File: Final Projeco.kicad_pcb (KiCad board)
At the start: 2 copper layers, 1 part, among them U1 ESP32-S3

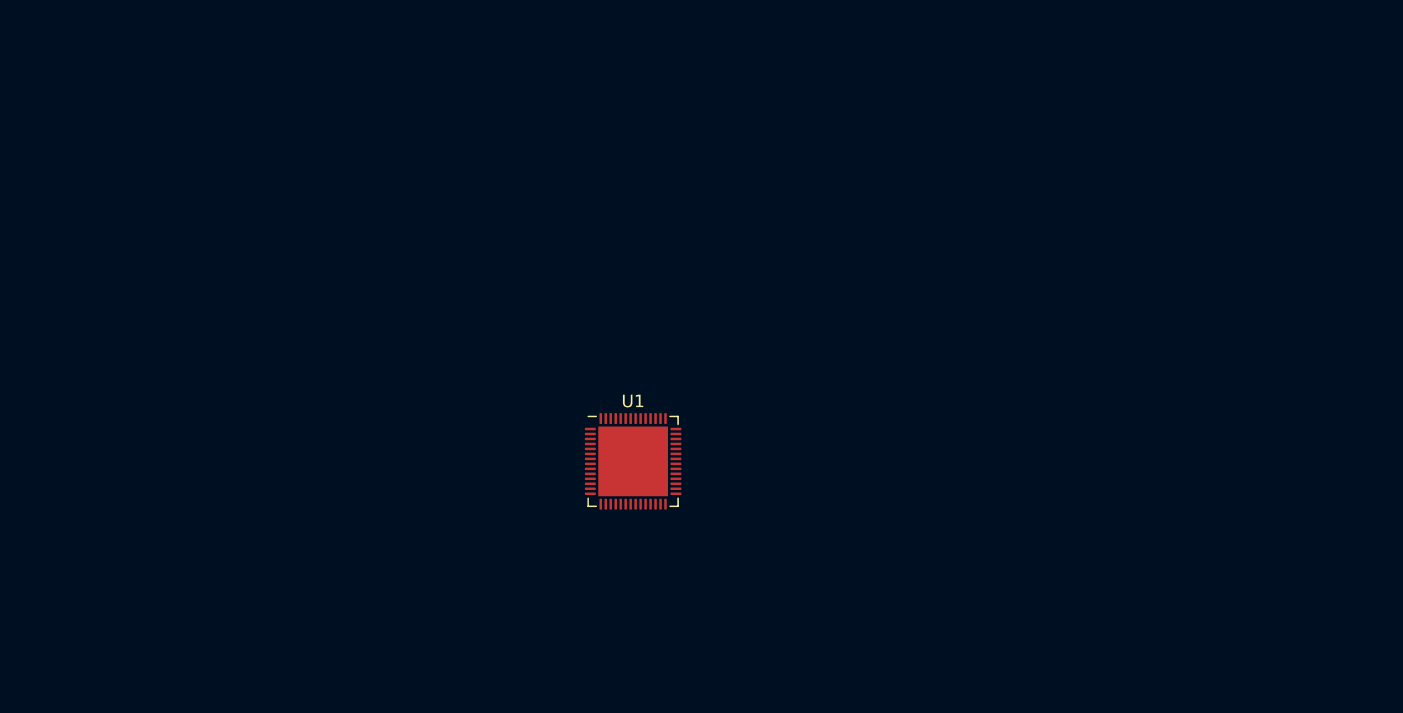
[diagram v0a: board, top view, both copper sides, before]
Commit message: -USE IPEX 2.4 GHz Antenna
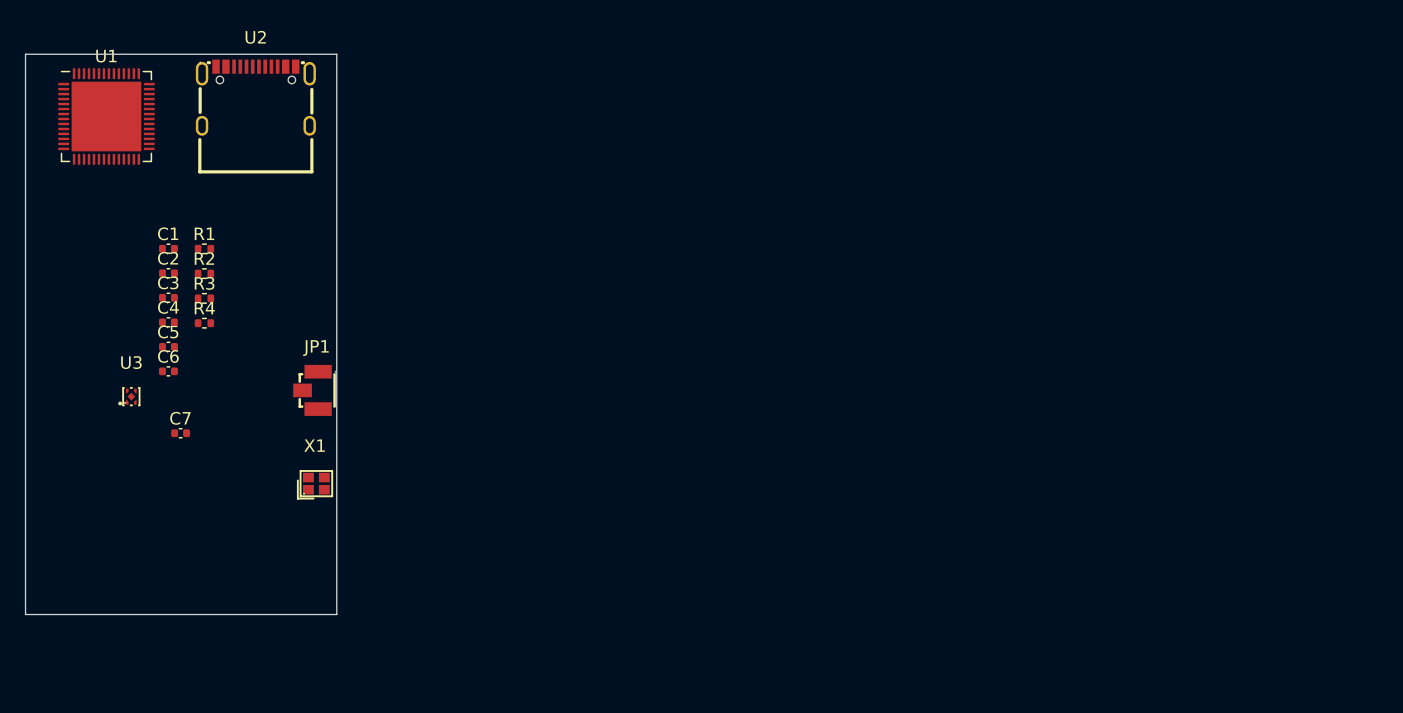
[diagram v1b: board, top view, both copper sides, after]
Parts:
- added C1: C, Capacitor_SMD:C_0402_1005Metric, F.Cu at (38.0, 31.1)
- added C2: C, Capacitor_SMD:C_0402_1005Metric, F.Cu at (38.0, 33.1)
- added C3: 1uF, Capacitor_SMD:C_0402_1005Metric, F.Cu at (38.0, 35.1)
- added C4: C, Capacitor_SMD:C_0402_1005Metric, F.Cu at (38.0, 37.0)
- added C5: C, Capacitor_SMD:C_0402_1005Metric, F.Cu at (38.0, 39.0)
- added C6: C, Capacitor_SMD:C_0402_1005Metric, F.Cu at (38.0, 41.0)
- added C7: 1uF, Capacitor_SMD:C_0402_1005Metric, F.Cu at (39.0, 45.9)
- added JP1: U_FL-R-SMT-1(10), jlc:ANT-SMD_UFL-R-SMT-1-10, F.Cu at (49.4, 42.5)
- added R1: 10K, Resistor_SMD:R_0402_1005Metric, F.Cu at (40.9, 31.1)
- added R2: 5.1K, Resistor_SMD:R_0402_1005Metric, F.Cu at (40.9, 33.1)
- added R3: 5.1K, Resistor_SMD:R_0402_1005Metric, F.Cu at (40.9, 35.1)
- added R4: 10K, Resistor_SMD:R_0402_1005Metric, F.Cu at (40.9, 37.1)
- added U2: GT-USB-7004N, jlc:USB-C-SMD_GT-USB-7004, F.Cu at (45.0, 18.9)
- added U3: NCP167BMX330TBG, jlc:XDFN-4_L1.0-W1.0-P0.65-BL-EP, F.Cu at (35.0, 43.0)
- added X1: TZ1269D, jlc:CRYSTAL-SMD_4P-L2.0-W1.6-BL-A, F.Cu at (49.9, 50.0)
- moved U1 50.6 mm to (33.0, 20.5)
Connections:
- U1 pad 1: unconnected-(U1-LNA_IN/RF-Pad1) -> Net-(JP1-SIN)
- U1 pad 57: unconnected-(U1-GND-Pad57) -> Net-(U1-GND)
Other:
- board outline added: 25 x 45 mm

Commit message: -Added some Headers
-Added Headers
-TODO (chore) (top priority):
 -    relabel EVERYTHING with net class (line) NOT directive (circle)
 -    get layout fixed
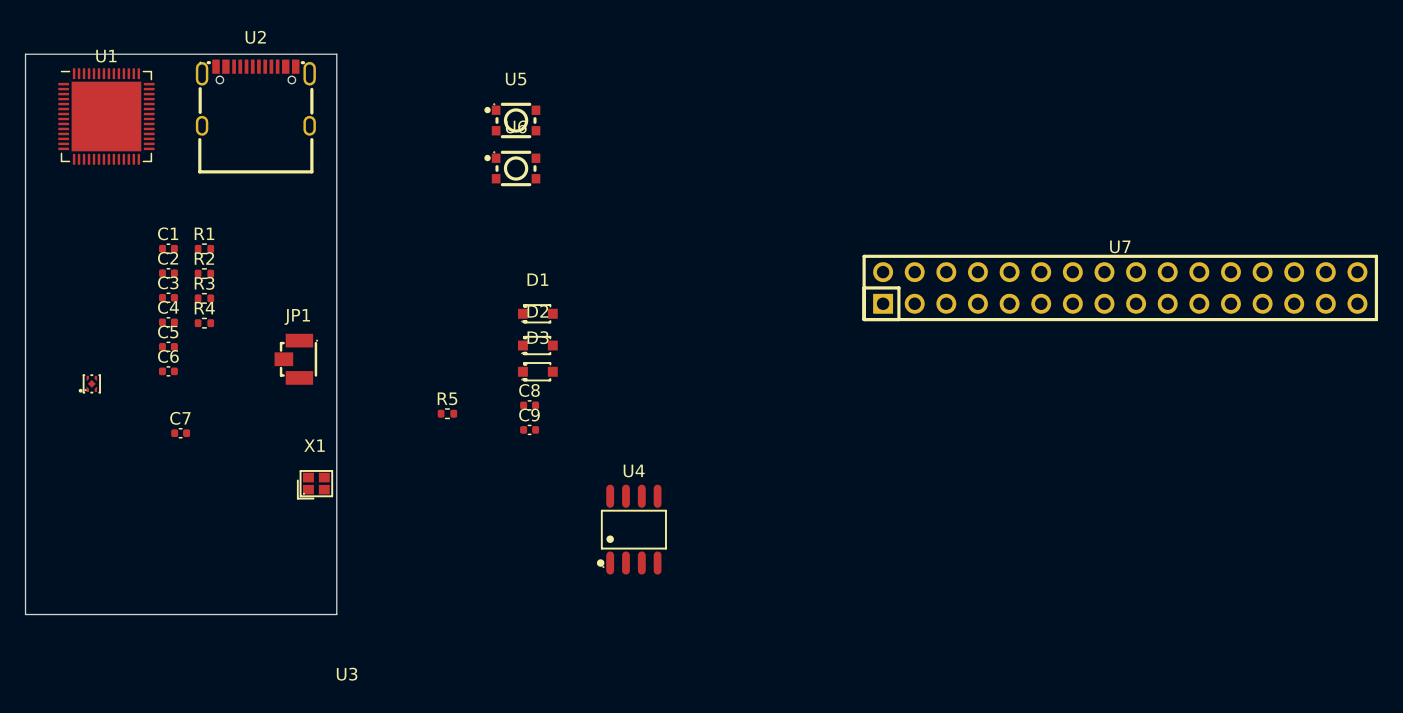
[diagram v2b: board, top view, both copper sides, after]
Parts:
- added C8: 1uF, Capacitor_SMD:C_0402_1005Metric, F.Cu at (67.0, 43.7)
- added C9: 0.1uF, Capacitor_SMD:C_0402_1005Metric, F.Cu at (67.0, 45.7)
- added D1: SD103AWS_C5345966, jlc:SOD-323_L1.7-W1.3-LS2.5-RD, F.Cu at (67.7, 36.3)
- added D2: SD103AWS_C5345966, jlc:SOD-323_L1.7-W1.3-LS2.5-RD, F.Cu at (67.7, 38.9)
- added D3: SD103AWS_C5345966, jlc:SOD-323_L1.7-W1.3-LS2.5-RD, F.Cu at (67.7, 41.0)
- added R5: 100K, Resistor_SMD:R_0402_1005Metric, F.Cu at (60.4, 44.4)
- added U4: LY68L6400SLIT, jlc:SOP-8_L4.9-W3.9-P1.27-LS6.0-BL, F.Cu at (75.4, 53.7)
- added U5: PTS830GG140SMTRLFS, jlc:KEY-SMD_4P-L3.1-W2.6_PTS830GG140SMTRLFS, F.Cu at (65.9, 20.8)
- added U6: PTS830GG140SMTRLFS, jlc:KEY-SMD_4P-L3.1-W2.6_PTS830GG140SMTRLFS, F.Cu at (65.9, 24.7)
- added U7: 220S-2*16P_H=8_5MM_Ytype_L=3_0MM_PBT, jlc:HDR-TH_32P-P2.54-V-F-R2-C16-S2.54, F.Cu at (114.4, 34.3)
- C4: value C -> 1u
- moved U3 3.34 mm to (31.8, 42.0)
- moved JP1 2.92 mm to (47.9, 40.0)
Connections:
- U1 pad 20: unconnected-(U1-VDD3P3_RTC-Pad20) -> VDD3P3
- U1 pad 29: unconnected-(U1-VDD_SPI-Pad29) -> VDD3P3
- U1 pad 46: unconnected-(U1-VDD3P3_CPU-Pad46) -> VDD3P3
- U1 pad 55: Net-(U1-VDDA-Pad55) -> VDD3P3
- U1 pad 56: Net-(U1-VDDA-Pad55) -> VDD3P3
- U1 pad 6: unconnected-(U1-GPIO1/ADC1_CH0-Pad6) -> /GPIO1
- U1 pad 7: unconnected-(U1-GPIO2/ADC1_CH1-Pad7) -> /GPIO2
- U1 pad 8: unconnected-(U1-GPIO3/ADC1_CH2-Pad8) -> /GPIO3
- U1 pad 9: unconnected-(U1-GPIO4/ADC1_CH3-Pad9) -> /GPIO4
- U2 pad 1: unconnected-(U2-SHELL-Pad1) -> GND
- U2 pad A6: unconnected-(U2-DP1-PadA6) -> Net-(D2-K)
- U2 pad A7: unconnected-(U2-DN1-PadA7) -> Net-(D3-K)
- U2 pad B6: unconnected-(U2-DP2-PadB6) -> Net-(D2-K)
- U2 pad B7: unconnected-(U2-DN2-PadB7) -> Net-(D3-K)
